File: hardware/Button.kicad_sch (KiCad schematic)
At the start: 12 parts, among them J13 Conn_01x05_Pin, J5 Conn_01x05_Pin, Q1 2N7002, Q10 2N7002, Q2 2N7002, Q3 2N7002, Q9 2N7002

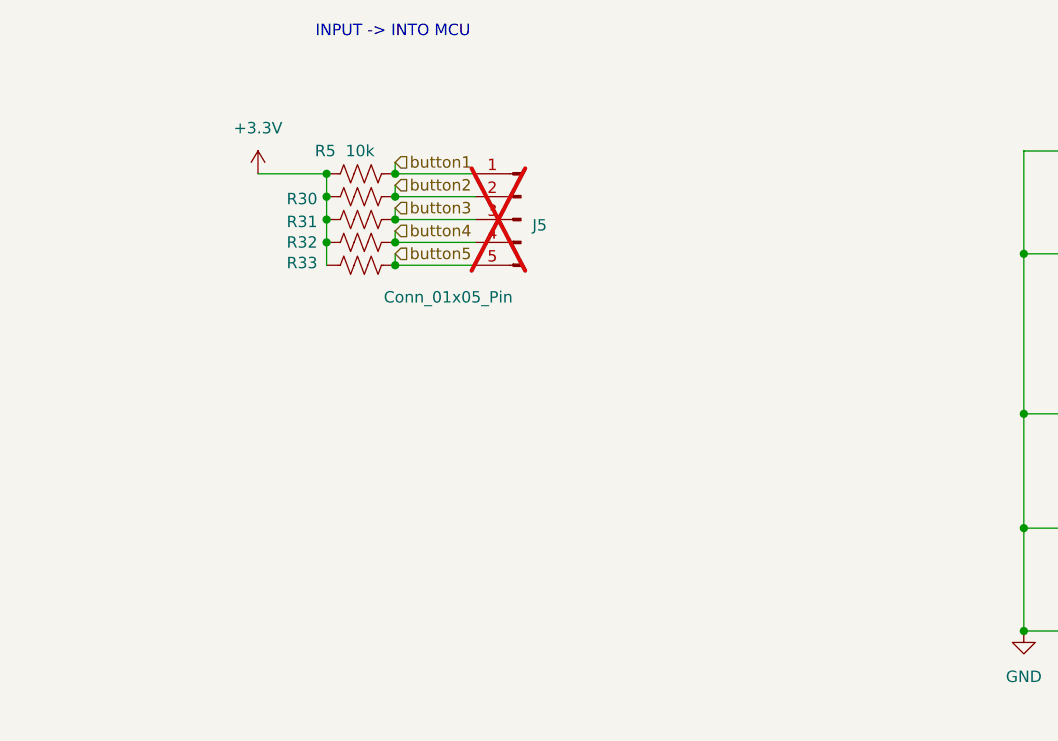
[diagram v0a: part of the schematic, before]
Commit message: Fixed ERC errors & CAN module
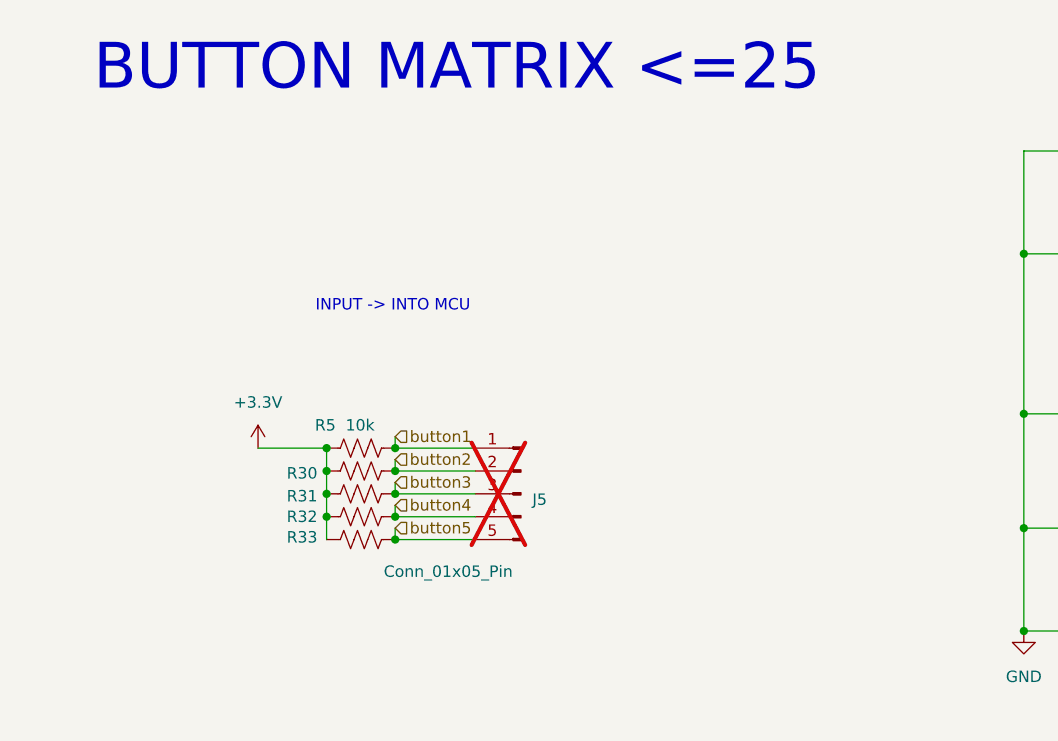
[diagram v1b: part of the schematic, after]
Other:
- note added: "BUTTON MATRIX <=25"
- moved on the sheet: J5, R30, R31, R32, R33, R5

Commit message: Added EEPROM, resolved comments
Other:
- company: (none) -> University of Toronto Human Powered Vehicles
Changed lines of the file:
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@@
 	(generator_version "9.0")
 	(paper "A5")
+	(title_block
+		(date "2025-08-20")
+		(rev "Rev5")
+		(company "University of Toronto Human Powered Vehicles")
+	)
 	(text "BUTTON MATRIX <=25"
 		(exclude_from_sim no)

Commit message: Stylistic changes
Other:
- moved on the sheet: J5, R30, R31, R32, R33, R5

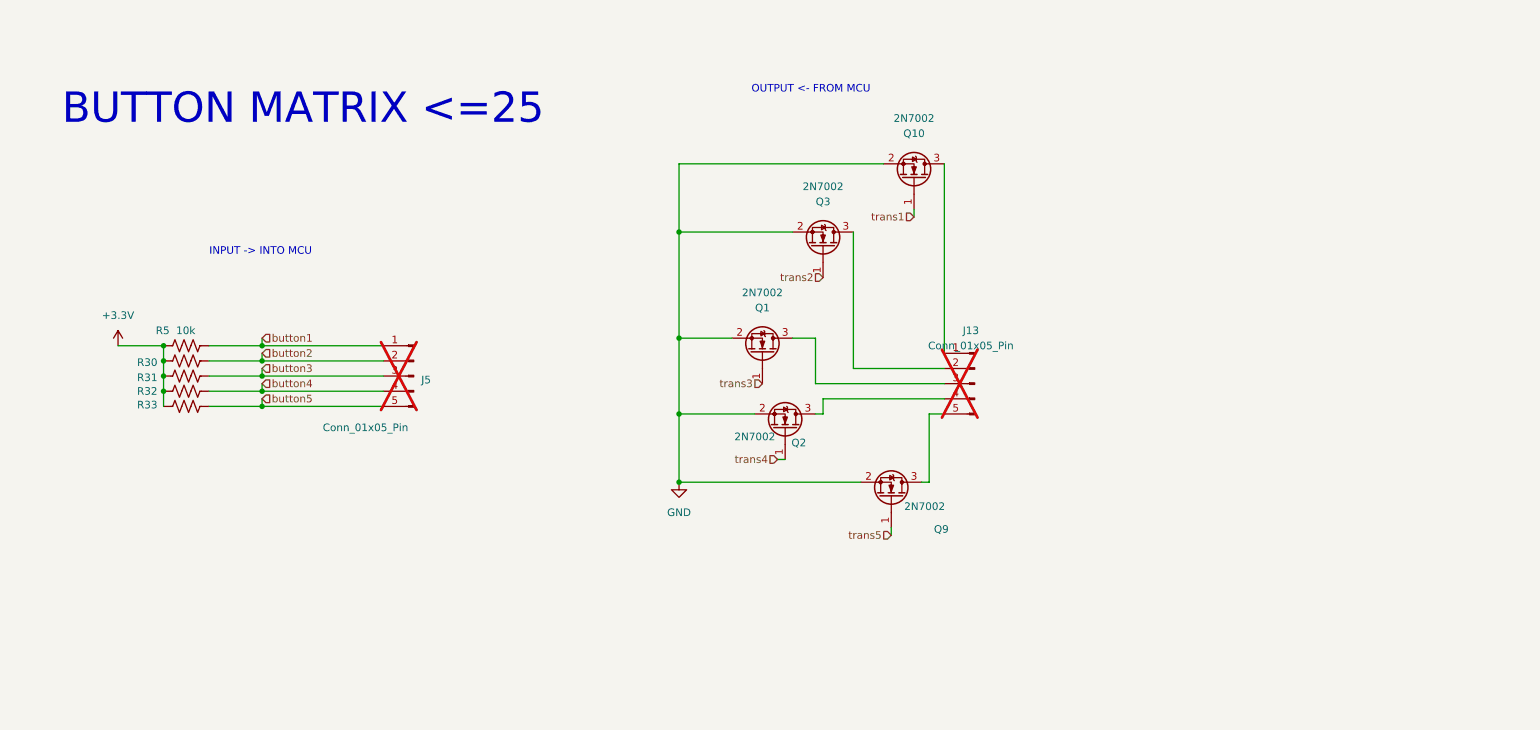
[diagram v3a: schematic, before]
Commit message: revamped button matrix
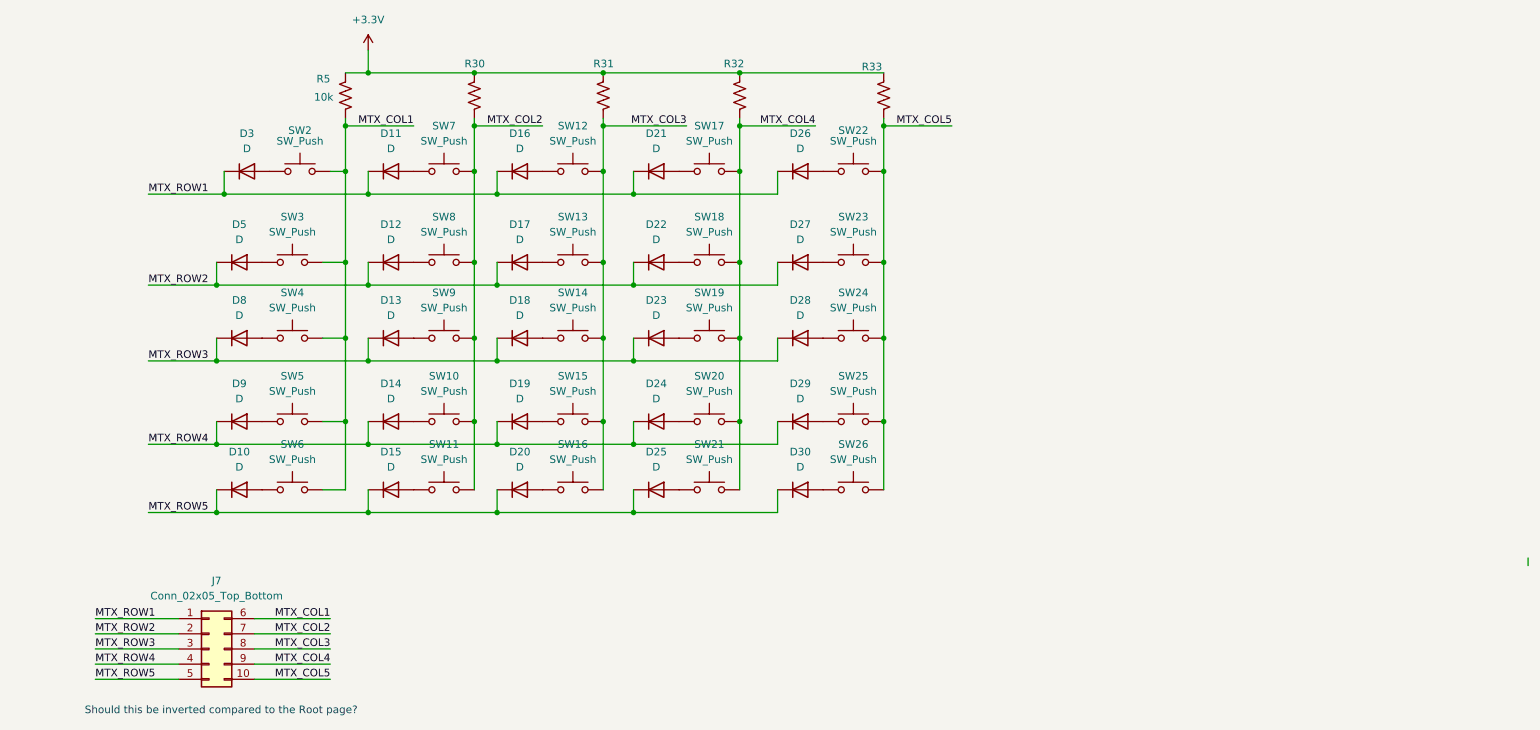
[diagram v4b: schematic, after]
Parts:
- removed J13, J5: Conn_01x05_Pin, Connector_PinHeader_2.54mm:PinHeader_1x05_P2.54mm_Vertical, symbol Connector:Conn_01x05_Pin
- removed Q1, Q10, Q2, Q3, Q9: 2N7002, Package_TO_SOT_SMD:SOT-23, symbol Transistor_FET:2N7002
- added D10, D11, D12, D13, D14, D15, D16, D17, D18, D19, D20, D21, D22, D23, D24, D25, D26, D27, D28, D29, D3, D30, D5, D8, D9: D, symbol Device:D
- added J7: Conn_02x05_Top_Bottom, symbol Connector_Generic:Conn_02x05_Top_Bottom
- added SW10, SW11, SW12, SW13, SW14, SW15, SW16, SW17, SW18, SW19, SW2, SW20, SW21, SW22, SW23, SW24, SW25, SW26, SW3, SW4, SW5, SW6, SW7, SW8, SW9: SW_Push, symbol Switch:SW_Push
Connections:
- net button1 renamed MTX_COL1
- net MTX_COL1: now also J7.6 (Pin_6), SW2.2, SW3.2, SW4.2, SW5.2, SW6.2
- net button2 renamed MTX_COL2
- net MTX_COL2: now also J7.7 (Pin_7), SW10.2, SW11.2, SW7.2, SW8.2, SW9.2
- net button3 renamed MTX_COL3
- net MTX_COL3: now also J7.8 (Pin_8), SW12.2, SW13.2, SW14.2, SW15.2, SW16.2
- net button4 renamed MTX_COL4
- net MTX_COL4: now also J7.9 (Pin_9), SW17.2, SW18.2, SW19.2, SW20.2, SW21.2
- net button5 renamed MTX_COL5
- net MTX_COL5: now also J7.10 (Pin_10), SW22.2, SW23.2, SW24.2, SW25.2, SW26.2
- new net: D28.2 (A), SW24.1
- new net: D3.2 (A), SW2.1
- new net: D19.2 (A), SW15.1
- new net: D12.2 (A), SW8.1
- new net: D26.2 (A), SW22.1
- new net: D27.2 (A), SW23.1
- new net: D10.2 (A), SW6.1
- new net: D21.2 (A), SW17.1
- new net: D11.2 (A), SW7.1
- new net: D20.2 (A), SW16.1
- new net: D18.2 (A), SW14.1
- new net: D16.2 (A), SW12.1
- new net: D15.2 (A), SW11.1
- new net: D9.2 (A), SW5.1
- new net: D13.2 (A), SW9.1
- new net: D29.2 (A), SW25.1
- new net: D23.2 (A), SW19.1
- new net: D17.2 (A), SW13.1
- new net: D25.2 (A), SW21.1
- new net: D8.2 (A), SW4.1
- new net: D5.2 (A), SW3.1
- new net: D14.2 (A), SW10.1
- new net: D22.2 (A), SW18.1
- new net: D24.2 (A), SW20.1
- new net: D30.2 (A), SW26.1
- new net MTX_ROW1: D11.1 (K), D16.1 (K), D21.1 (K), D26.1 (K), D3.1 (K), J7.1 (Pin_1)
- new net MTX_ROW2: D12.1 (K), D17.1 (K), D22.1 (K), D27.1 (K), D5.1 (K), J7.2 (Pin_2)
- new net MTX_ROW3: D13.1 (K), D18.1 (K), D23.1 (K), D28.1 (K), D8.1 (K), J7.3 (Pin_3)
- new net MTX_ROW4: D14.1 (K), D19.1 (K), D24.1 (K), D29.1 (K), D9.1 (K), J7.4 (Pin_4)
- new net MTX_ROW5: D10.1 (K), D15.1 (K), D20.1 (K), D25.1 (K), D30.1 (K), J7.5 (Pin_5)
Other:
- note added: "Should this be inverted compared to the Root page?"
- note removed: "BUTTON MATRIX <=25"
- note removed: "INPUT -> INTO MCU"
- note removed: "OUTPUT <- FROM MCU"
- moved on the sheet: R30, R31, R32, R33, R5

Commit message: Finished footprint assignment and deleted pcb
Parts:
- D10, D11, D12, D13, D14, D15, D16, D17, D18, D19, D20, D21, D22, D23, D24, D25, D26, D27, D28, D29, D30, D5, D8, D9: footprint (none) -> Diode_SMD:D_SOD-123
- D3: footprint (none) -> Diode_SMD:D_SOD-123; LCSC (none) -> C7422628
- J7: footprint (none) -> Connector_JST:JST_J2100_B10B-J21DK-GGXR_2x05_P2.50x4.00mm_Vertical
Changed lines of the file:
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@@
 			)
 		)
-		(property "Footprint" ""
+		(property "Footprint" "Diode_SMD:D_SOD-123"
 			(at 80.01 55.88 0)
 			(effects
@@
 			)
 		)
-		(property "Footprint" ""
+		(property "Footprint" "Diode_SMD:D_SOD-123"
 			(at 148.59 55.88 0)
 			(effects
@@
 			)
 		)
-		(property "Footprint" ""
+		(property "Footprint" "Diode_SMD:D_SOD-123"
 			(at 54.61 93.98 0)
 			(effects
@@
 			)
 		)
-		(property "Footprint" ""
+		(property "Footprint" "Diode_SMD:D_SOD-123"
 			(at 124.46 40.64 0)
 			(effects
@@
 			)
 		)
-		(property "Footprint" ""
+		(property "Footprint" "Diode_SMD:D_SOD-123"
 			(at 80.01 40.64 0)
 			(effects
@@
 			)
 		)
-		(property "Footprint" ""
+		(property "Footprint" "Diode_SMD:D_SOD-123"
 			(at 101.6 68.58 0)
 			(effects
@@
 			)
 		)
-		(property "Footprint" ""
+		(property "Footprint" "Diode_SMD:D_SOD-123"
 			(at 101.6 40.64 0)
 			(effects
@@
 			)
 		)
-		(property "Footprint" ""
+		(property "Footprint" "Diode_SMD:D_SOD-123"
 			(at 80.01 93.98 0)
 			(effects
@@
 			)
 		)
-		(property "Footprint" ""
+		(property "Footprint" "Diode_SMD:D_SOD-123"
 			(at 54.61 82.55 0)
 			(effects
@@
 			)
 		)
-		(property "Footprint" ""
+		(property "Footprint" "Diode_SMD:D_SOD-123"
 			(at 80.01 68.58 0)
 			(effects
@@
 			)
 		)
-		(property "Footprint" ""
+		(property "Footprint" "Diode_SMD:D_SOD-123"
 			(at 101.6 93.98 0)
 			(effects
@@
 			)
 		)
-		(property "Footprint" ""
+		(property "Footprint" "Connector_JST:JST_J2100_B10B-J21DK-GGXR_2x05_P2.50x4.00mm_Vertical"
 			(at 49.53 120.65 0)
 			(effects
@@
 			)
 		)
-		(property "Footprint" ""
+		(property "Footprint" "Diode_SMD:D_SOD-123"
 			(at 148.59 82.55 0)
 			(effects
@@
 			)
 		)
-		(property "Footprint" ""
+		(property "Footprint" "Diode_SMD:D_SOD-123"
 			(at 124.46 68.58 0)
 			(effects
@@
 			)
 		)
-		(property "Footprint" ""
+		(property "Footprint" "Diode_SMD:D_SOD-123"
 			(at 55.88 40.64 0)
 			(effects
@@
 			)
 		)
-		(property "Datasheet" "~"
+		(property "Datasheet" "https://www.lcsc.com/datasheet/C7422628.pdf"
 			(at 55.88 40.64 0)
 			(effects
@@
 			)
 		)
+		(property "LCSC" "C7422628"
+			(at 55.88 40.64 0)
+			(effects
+				(font
+					(size 1.27 1.27)
+				)
+				(hide yes)
+			)
+		)
 		(pin "1"
 		)
@@
 			)
 		)
-		(property "Footprint" ""
+		(property "Footprint" "Diode_SMD:D_SOD-123"
 			(at 54.61 68.58 0)
 			(effects
@@
 			)
 		)
-		(property "Footprint" ""
+		(property "Footprint" "Diode_SMD:D_SOD-123"
 			(at 101.6 82.55 0)
 			(effects
@@
 			)
 		)
-		(property "Footprint" ""
+		(property "Footprint" "Diode_SMD:D_SOD-123"
 			(at 54.61 55.88 0)
 			(effects
@@
 			)
 		)
-		(property "Footprint" ""
+		(property "Footprint" "Diode_SMD:D_SOD-123"
 			(at 148.59 68.58 0)
 			(effects
@@
 			)
 		)
-		(property "Footprint" ""
+		(property "Footprint" "Diode_SMD:D_SOD-123"
 			(at 124.46 82.55 0)
 			(effects
@@
 			)
 		)
-		(property "Footprint" ""
+		(property "Footprint" "Diode_SMD:D_SOD-123"
 			(at 124.46 93.98 0)
 			(effects
@@
 			)
 		)
-		(property "Footprint" ""
+		(property "Footprint" "Diode_SMD:D_SOD-123"
 			(at 148.59 40.64 0)
 			(effects
@@
 			)
 		)
-		(property "Footprint" ""
+		(property "Footprint" "Diode_SMD:D_SOD-123"
 			(at 124.46 55.88 0)
 			(effects
@@
 			)
 		)
-		(property "Footprint" ""
+		(property "Footprint" "Diode_SMD:D_SOD-123"
 			(at 148.59 93.98 0)
 			(effects
@@
 			)
 		)
-		(property "Footprint" ""
+		(property "Footprint" "Diode_SMD:D_SOD-123"
 			(at 80.01 82.55 0)
 			(effects
@@
 			)
 		)
-		(property "Footprint" ""
+		(property "Footprint" "Diode_SMD:D_SOD-123"
 			(at 101.6 55.88 0)
 			(effects

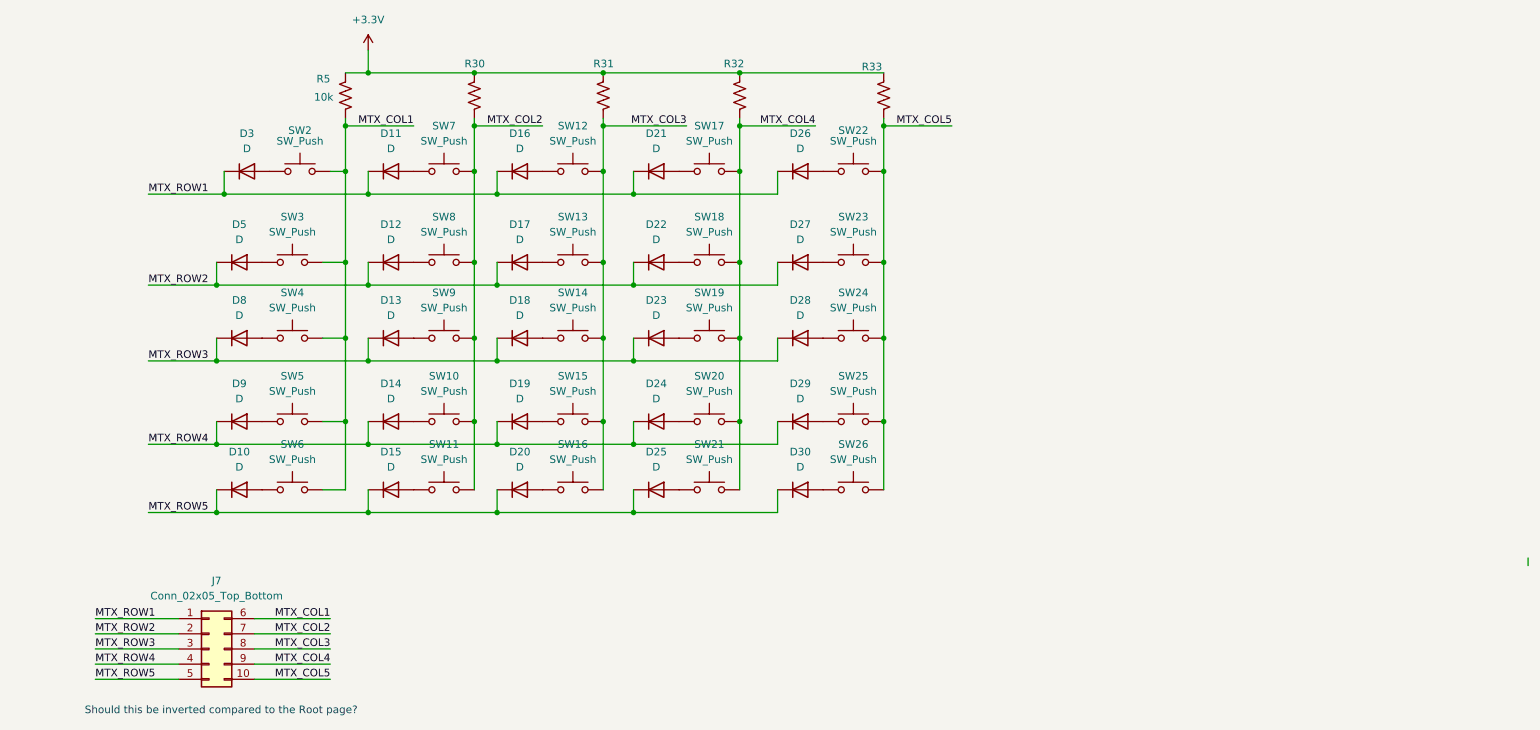
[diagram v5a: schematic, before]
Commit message: modified mcu pin alloc and pre-routing placement
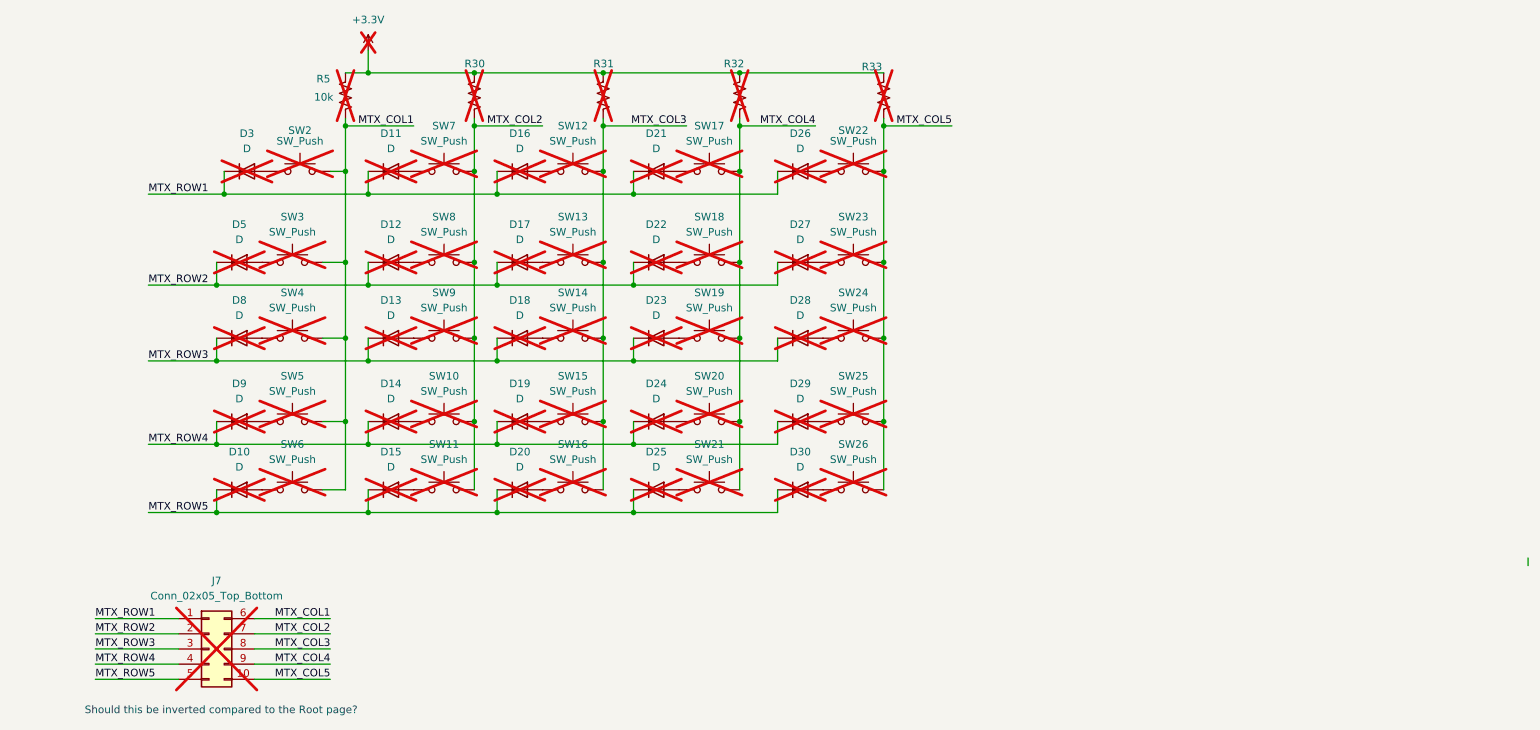
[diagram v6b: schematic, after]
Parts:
- D10, D11, D12, D13, D14, D15, D16, D17, D18, D19, D20, D21, D22, D23, D24, D25, D26, D27, D28, D29, D3, D30, D5, D8, D9, J7, R30, R31, R32, R33, R5, SW10, SW11, SW12, SW13, SW14, SW15, SW16, SW17, SW18, SW19, SW2, SW20, SW21, SW22, SW23, SW24, SW25, SW26, SW3, SW4, SW5, SW6, SW7, SW8, SW9: now not fitted

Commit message: Completed first layout draft
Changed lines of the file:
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@@
-	(wire
-		(pts
-			(xy 270.51 106.68) (xy 270.51 105.41)
-		)
-		(stroke
-			(width 0)
-			(type default)
-		)
-	)
 	(wire
 		(pts

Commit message: Resolved comments
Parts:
- D3: LCSC C7422628 -> (none)
- J7: LCSC (none) -> C471519
- R30, R31, R32, R33, R5: LCSC C25804 -> C98220
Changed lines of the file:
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@@
 			)
 		)
-		(property "LCSC" "C25804"
+		(property "LCSC" "C98220"
 			(at 115.57 27.94 0)
 			(effects
@@
 			)
 		)
+		(property "LCSC" "C471519"
+			(at 49.53 120.65 0)
+			(effects
+				(font
+					(size 1.27 1.27)
+				)
+				(hide yes)
+			)
+		)
 		(pin "1"
 		)
@@
 			)
 		)
-		(property "LCSC" "C7422628"
+		(property "LCSC" ""
 			(at 55.88 40.64 0)
 			(effects
@@
 			)
 		)
-		(property "LCSC" "C25804"
+		(property "LCSC" "C98220"
 			(at 72.39 27.94 0)
 			(effects
@@
 			)
 		)
-		(property "LCSC" "C25804"
+		(property "LCSC" "C98220"
 			(at 162.56 27.94 0)
 			(effects
@@
 			)
 		)
-		(property "LCSC" "C25804"
+		(property "LCSC" "C98220"
 			(at 138.43 27.94 0)
 			(effects
@@
 			)
 		)
-		(property "LCSC" "C25804"
+		(property "LCSC" "C98220"
 			(at 93.98 27.94 0)
 			(effects
